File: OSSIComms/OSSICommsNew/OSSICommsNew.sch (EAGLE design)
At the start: 188 parts, among them Q1 NX-3215, U1 MAX2640, U10 MAX6369, U11 TPS3838, U12 MAX890L, U13 MCP1700_SOT23, U2 PE4259, U3 RF5110G, U4 OPA347, U5 MAX869L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

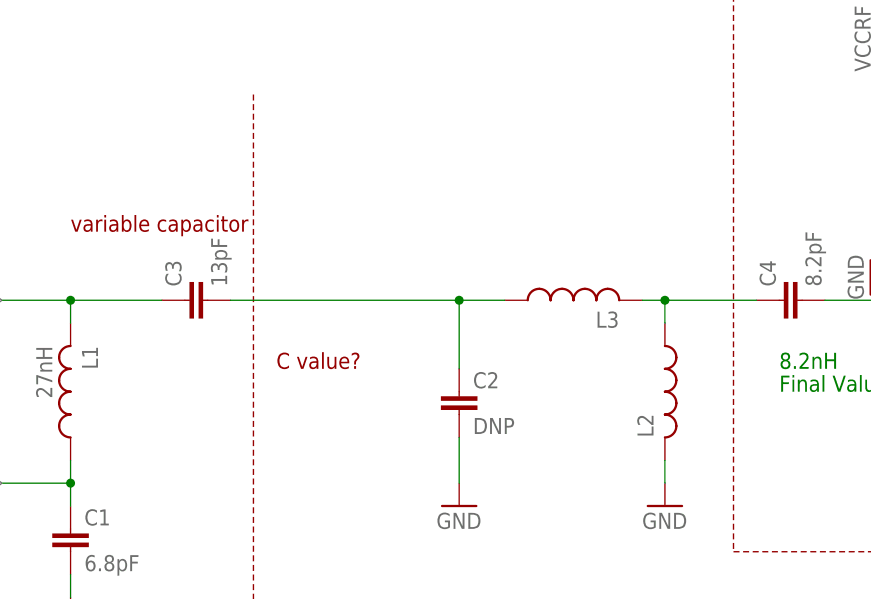
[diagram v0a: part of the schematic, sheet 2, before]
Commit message: some library description updated
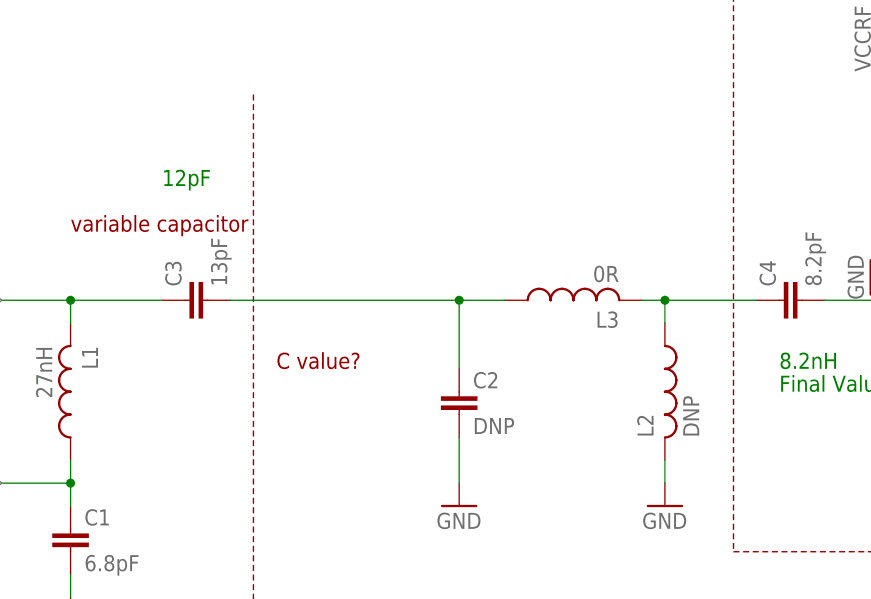
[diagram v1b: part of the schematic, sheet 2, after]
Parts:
- L2: value (none) -> DNP
- L3: value (none) -> 0R
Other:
- note added: "12pF"
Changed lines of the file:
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@@
 <part name="R1" library="OSSI" deviceset="R" device="0603(1608)" value="100k"/>
 <part name="GND21" library="OSSI" deviceset="GND" device=""/>
-<part name="L3" library="OSSI" deviceset="L" device="0603(1608)"/>
+<part name="L3" library="OSSI" deviceset="L" device="0603(1608)" value="0R"/>
 <part name="C2" library="OSSI" deviceset="C" device="0603(1608)" value="DNP"/>
-<part name="L2" library="OSSI" deviceset="L" device="0603(1608)"/>
+<part name="L2" library="OSSI" deviceset="L" device="0603(1608)" value="DNP"/>
 <part name="GND24" library="OSSI" deviceset="GND" device=""/>
 <part name="GND25" library="OSSI" deviceset="GND" device=""/>
@@
 <text x="116.84" y="45.72" size="1.778" layer="91">8.2nH</text>
 <text x="116.84" y="43.18" size="1.778" layer="91">Final Value but the result will be similar</text>
+<text x="48.26" y="66.04" size="1.778" layer="91">12pF</text>
 </plain>
 <instances>

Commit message: design file are added / missing values are added
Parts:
- C10, C15, C9: value (none) -> 56pF
- C41: value (none) -> 4.7uF
- C44: value 100uF,1210 -> 4.7uF,1210
- C45: value (none) -> 22uF
- C46: value (none) -> 100uF
- L4: value (none) -> DNP
- L6: value (none) -> 0R
- R11: value TBD -> 750R
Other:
- note added: "Ground is shared but the ground plane is carefully layouted"
- note added: "OPA347 is changed to LM7321 and a jumper wire is used to complete the circuit!!"
- note added: "Set current limit = ~ 1.6A"
- note added: "Set to 2.8V for 1W RF power and best efficiency!!!"
- note removed: "Change this to LM7321"
- note removed: "Set to 2.25V for 1W and best efficiency!!!"
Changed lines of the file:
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@@
 <?xml version="1.0" encoding="utf-8"?>
 <!DOCTYPE eagle SYSTEM "eagle.dtd">
-<eagle version="6.1">
+<eagle version="6.5.0">
 <drawing>
 <settings>
@@
 <part name="L10" library="OSSI" deviceset="L" device="0603(1608)" value="0R"/>
 <part name="L8" library="OSSI" deviceset="L" device="0603(1608)" value="0R"/>
-<part name="L6" library="OSSI" deviceset="L" device="0603(1608)"/>
-<part name="L4" library="OSSI" deviceset="L" device="0603(1608)"/>
+<part name="L6" library="OSSI" deviceset="L" device="0603(1608)" value="0R"/>
+<part name="L4" library="OSSI" deviceset="L" device="0603(1608)" value="DNP"/>
 <part name="C5" library="OSSI" deviceset="C" device="0603(1608)" value="DNP"/>
 <part name="C17" library="OSSI" deviceset="C" device="0603(1608)" value="DNP"/>
@@
 <part name="GND49" library="OSSI" deviceset="GND" device=""/>
 <part name="C42" library="OSSI" deviceset="C" device="1210(3225)-GCM32" value="22uF,1210"/>
-<part name="C46" library="OSSI" deviceset="C" device="1210(3225)-GCM32"/>
-<part name="C45" library="OSSI" deviceset="C" device="1210(3225)-GCM32"/>
-<part name="C41" library="OSSI" deviceset="C" device="1210(3225)-GCM32"/>
-<part name="C44" library="OSSI" deviceset="C" device="0805(2012)" value="100uF,1210"/>
+<part name="C46" library="OSSI" deviceset="C" device="1210(3225)-GCM32" value="100uF"/>
+<part name="C45" library="OSSI" deviceset="C" device="1210(3225)-GCM32" value="22uF"/>
+<part name="C41" library="OSSI" deviceset="C" device="1210(3225)-GCM32" value="4.7uF"/>
+<part name="C44" library="OSSI" deviceset="C" device="0805(2012)" value="4.7uF,1210"/>
 <part name="GND50" library="OSSI" deviceset="GND" device=""/>
 <part name="GND51" library="OSSI" deviceset="GND" device=""/>
@@
 <part name="R6" library="OSSI" deviceset="R" device="0603(1608)" value="4.12k"/>
 <part name="GND53" library="OSSI" deviceset="GND" device=""/>
-<part name="R11" library="OSSI" deviceset="R" device="0603(1608)" value="TBD"/>
+<part name="R11" library="OSSI" deviceset="R" device="0603(1608)" value="750R"/>
 <part name="GND54" library="OSSI" deviceset="GND" device=""/>
 <part name="GND55" library="OSSI" deviceset="GND" device=""/>
@@
 <part name="R2" library="OSSI" deviceset="R" device="0603(1608)" value="1.5k"/>
 <part name="R3" library="OSSI" deviceset="R" device="0603(1608)" value="1.5k"/>
-<part name="C15" library="OSSI" deviceset="C" device="0603(1608)"/>
-<part name="C9" library="OSSI" deviceset="C" device="0603(1608)"/>
+<part name="C15" library="OSSI" deviceset="C" device="0603(1608)" value="56pF"/>
+<part name="C9" library="OSSI" deviceset="C" device="0603(1608)" value="56pF"/>
 <part name="GND20" library="OSSI" deviceset="GND" device=""/>
 <part name="VCCRF15" library="OSSI" deviceset="VCCRF" device=""/>
@@
 <part name="GND25" library="OSSI" deviceset="GND" device=""/>
 <part name="GND30" library="OSSI" deviceset="GND" device=""/>
-<part name="C10" library="OSSI" deviceset="C" device="0603(1608)"/>
+<part name="C10" library="OSSI" deviceset="C" device="0603(1608)" value="56pF"/>
 <part name="R29" library="OSSI" deviceset="R" device="0603(1608)" value="4.7k"/>
 <part name="R28" library="OSSI" deviceset="R" device="0603(1608)" value="4.7k"/>
@@
 <text x="30.48" y="160.02" size="1.778" layer="94" rot="R90">Eval board settng is 13nH &amp; 10pF</text>
 <text x="322.58" y="190.5" size="1.778" layer="94">Set VCOMMS_PA to 3.3~3.4V</text>
-<text x="106.68" y="215.9" size="1.778" layer="94">Current drive capability should be larger!!!</text>
-<text x="106.68" y="213.36" size="1.778" layer="94">Change this to LM7321</text>
-<text x="106.68" y="205.74" size="1.778" layer="94">Set to 2.25V for 1W and best efficiency!!!</text>
+<text x="78.74" y="259.08" size="1.778" layer="94">Current drive capability should be larger!!!</text>
+<text x="78.74" y="254" size="2.54" layer="94">OPA347 is changed to LM7321 and a jumper wire is used to complete the circuit!!</text>
+<text x="106.68" y="205.74" size="1.778" layer="94">Set to 2.8V for 1W RF power and best efficiency!!!</text>
 <text x="200.66" y="93.98" size="1.778" layer="94">Use Tantal for larger RF out</text>
 <text x="256.54" y="190.5" size="1.778" layer="94">Use Tantal for larger RF out</text>
@@
 <text x="116.84" y="43.18" size="1.778" layer="91">Final Value but the result will be similar</text>
 <text x="48.26" y="66.04" size="1.778" layer="91">12pF</text>
+<text x="238.76" y="203.2" size="1.778" layer="94">Set current limit = ~ 1.6A</text>
 </plain>
 <instances>
@@
 <text x="281.94" y="246.38" size="1.778" layer="94">DIGITAL / RF POWER CHOKE</text>
 <text x="114.3" y="190.5" size="1.778" layer="94">222.5mA limit</text>
+<text x="269.24" y="208.28" size="1.778" layer="94">Ground is shared but the ground plane is carefully layouted</text>
 </plain>
 <instances>
